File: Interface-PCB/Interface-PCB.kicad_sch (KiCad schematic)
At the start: 14 parts, among them J1 BARREL_JACK_PAD, J2 BARREL_JACK_PAD, J3 GPIO_DEBUG_HEADER, J4 RASPBERRYPI_GPIO_CONN_HEADER, J5 I2C_HEADER, M1 PERISTALTIC_PUMP, M2 PERISTALTIC_PUMP, M3 PERISTALTIC_PUMP, U1 TB6612FNG_BREAKOUT, U2 TB6612FNG_BREAKOUT

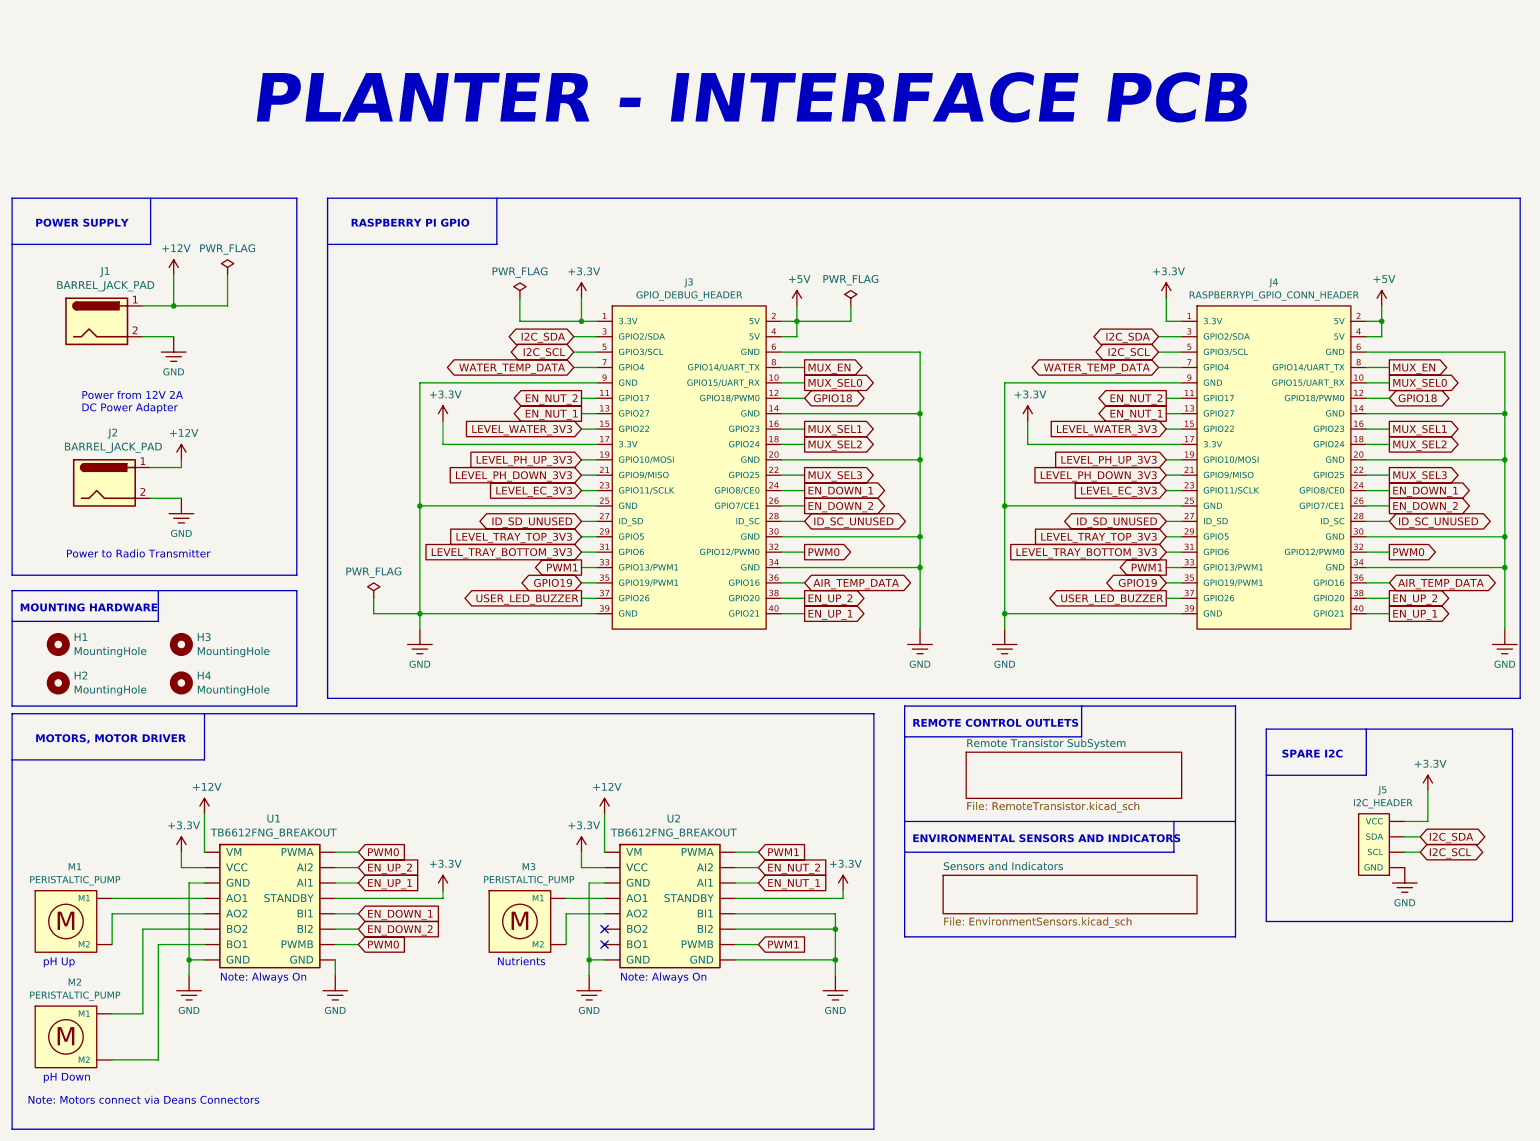
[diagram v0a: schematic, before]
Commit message: Update schematic based on breadboard tests
- Add current limiting resistors to Level Shifter output
- Add pull down resistors on all Mux outputs
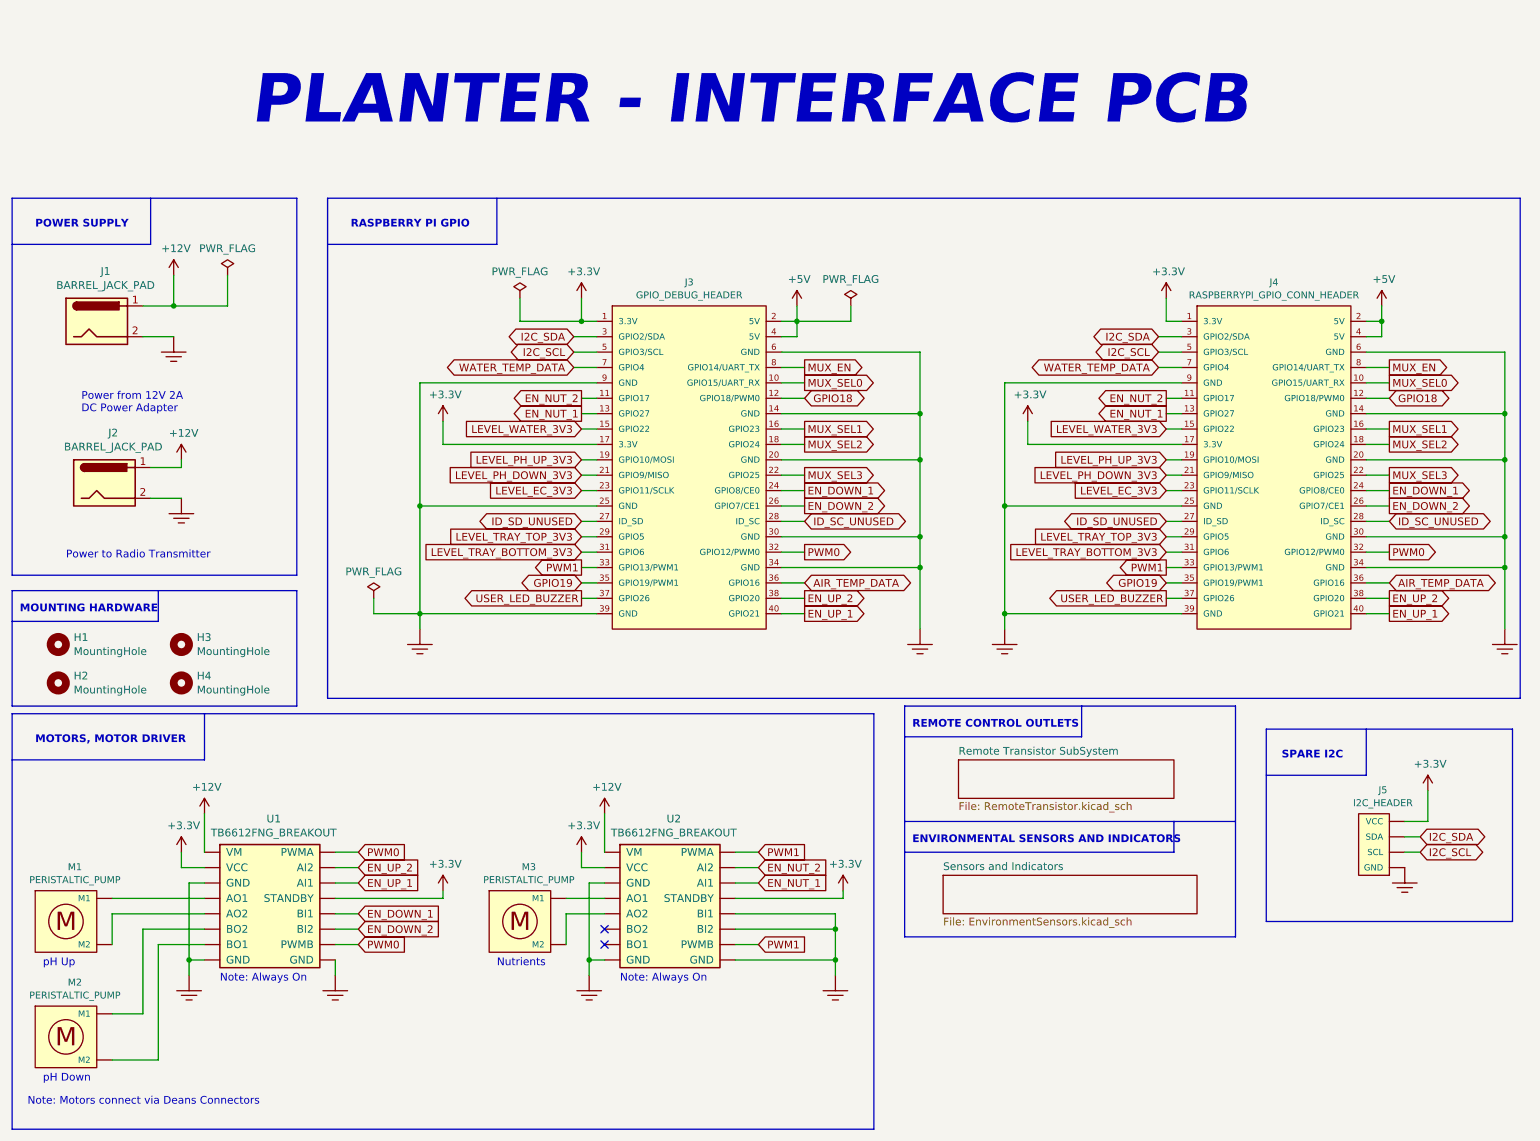
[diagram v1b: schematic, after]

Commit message: Add Planter Logo to schematic
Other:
- note added: "INTERFACE PCB"
- note removed: "PLANTER - INTERFACE PCB"
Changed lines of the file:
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@@
     (effects (font (size 1.27 1.27)) (justify left bottom))
   )
-  (text "PLANTER - INTERFACE PCB" (at 54.61 36.83 0)
+  (text "INTERFACE PCB" (at 93.98 38.1 0)
     (effects (font (size 8.001 8.001) (thickness 1.6002) bold italic) (justify left bottom))
   )
@@
     (pin "~")
   )
+  (symbol (lib_id "Interface-PCB:PLANTER_LOGO_8mm") (at 247.65 29.21 0) (unit 1)
+    (in_bom yes) (on_board yes) (fields_autoplaced)
+    (property "Reference" "#G1" (id 0) (at 247.65 17.3277 0)
+      (effects (font (size 1.27 1.27)) hide)
+    )
+    (property "Value" "PLANTER_LOGO_8mm" (id 1) (at 247.65 41.0923 0)
+      (effects (font (size 1.27 1.27)) hide)
+    )
+    (property "Footprint" "" (id 2) (at 247.65 29.21 0)
+      (effects (font (size 1.27 1.27)) hide)
+    )
+    (property "Datasheet" "" (id 3) (at 247.65 29.21 0)
+      (effects (font (size 1.27 1.27)) hide)
+    )
+  )
   (sheet (at 171.45 140.97) (size 35.56 6.35) (fields_autoplaced)
     (stroke (width 0) (type solid) (color 0 0 0 0))
@@
       (reference "#FLG04") (unit 1) (value "PWR_FLAG") (footprint "")
     )
+    (path "/6ae23f34-90ad-41bf-a46e-855f1c65bb29"
+      (reference "#G1") (unit 1) (value "PLANTER_LOGO_8mm") (footprint "")
+    )
     (path "/00000000-0000-0000-0000-000063fcc8a0"

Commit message: Add footprints for pads
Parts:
- J1, J2, M1, M2, M3: footprint TestPoint:TestPoint_2Pads_Pitch5.08mm_Drill1.3mm -> AA_Custom_Components:PowerPad_Pair_5.0x5.0mm
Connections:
- net at U1.4 (AO1): now also M1.1 (M1); no longer M1.7 (M1)
- net at U1.5 (AO2): now also M1.2 (M2); no longer M1.6 (M2)
- net at U1.6 (BO2): now also M2.1 (M1); no longer M2.7 (M1)
- net at U1.7 (BO1): now also M2.2 (M2); no longer M2.6 (M2)
- net at U2.4 (AO1): now also M3.1 (M1); no longer M3.7 (M1)
- net at U2.5 (AO2): now also M3.2 (M2); no longer M3.6 (M2)

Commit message: Add breakout board and IC footprints
- MUX
- Motor Driver
- PDIP ICs
- LEDs
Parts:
- U1, U2: footprint digikey-footprints:DIP-16_W7.62mm -> AA_Custom_Components:TB6612FNG_Breakout; Digikey_Part_Number (none) -> 1568-1755-ND; Manufacturer_Name (none) -> SparkFun
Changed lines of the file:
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@@
     (property "Reference" "U1" (id 0) (at 58.42 150.6982 0))
     (property "Value" "TB6612FNG_BREAKOUT" (id 1) (at 58.42 153.0096 0))
-    (property "Footprint" "digikey-footprints:DIP-16_W7.62mm" (id 2) (at 44.45 160.02 0)
+    (property "Footprint" "AA_Custom_Components:TB6612FNG_Breakout" (id 2) (at 44.45 160.02 0)
       (effects (font (size 1.27 1.27)) (justify left) hide)
     )
-    (property "Datasheet" "" (id 3) (at 62.23 160.02 0)
+    (property "Datasheet" "https://media.digikey.com/pdf/Data%20Sheets/Sparkfun%20PDFs/ROB-14450_Web.pdf" (id 3) (at 62.23 160.02 0)
+      (effects (font (size 1.27 1.27)) hide)
+    )
+    (property "Manufacturer_Name" "SparkFun" (id 4) (at 74.93 166.37 0)
+      (effects (font (size 1.27 1.27)) hide)
+    )
+    (property "Digikey_Part_Number" "1568-1755-ND" (id 5) (at 78.74 168.91 0)
       (effects (font (size 1.27 1.27)) hide)
     )
@@
     (property "Reference" "U2" (id 0) (at 124.46 150.6982 0))
     (property "Value" "TB6612FNG_BREAKOUT" (id 1) (at 124.46 153.0096 0))
-    (property "Footprint" "digikey-footprints:DIP-16_W7.62mm" (id 2) (at 110.49 160.02 0)
+    (property "Footprint" "AA_Custom_Components:TB6612FNG_Breakout" (id 2) (at 110.49 160.02 0)
       (effects (font (size 1.27 1.27)) (justify left) hide)
     )
-    (property "Datasheet" "" (id 3) (at 128.27 160.02 0)
+    (property "Datasheet" "https://media.digikey.com/pdf/Data%20Sheets/Sparkfun%20PDFs/ROB-14450_Web.pdf" (id 3) (at 128.27 160.02 0)
+      (effects (font (size 1.27 1.27)) hide)
+    )
+    (property "Manufacturer_Name" "SparkFun" (id 4) (at 140.97 166.37 0)
+      (effects (font (size 1.27 1.27)) hide)
+    )
+    (property "Digikey_Part_Number" "1568-1755-ND" (id 5) (at 144.78 168.91 0)
       (effects (font (size 1.27 1.27)) hide)
     )
@@
       (effects (font (size 1.27 1.27)) hide)
     )
-    (property "Datasheet" "~" (id 3) (at 30.48 69.596 0)
+    (property "Datasheet" "" (id 3) (at 30.48 69.596 0)
       (effects (font (size 1.27 1.27)) hide)
     )
@@
       (effects (font (size 1.27 1.27)) hide)
     )
-    (property "Datasheet" "~" (id 3) (at 31.75 96.266 0)
+    (property "Datasheet" "" (id 3) (at 31.75 96.266 0)
       (effects (font (size 1.27 1.27)) hide)
     )
@@
     )
     (path "/00000000-0000-0000-0000-00006375997b/00000000-0000-0000-0000-000063bcadd9"
-      (reference "D2") (unit 1) (value "12V_ON_SMD") (footprint "LED_SMD:LED_1206_3216Metric_Pad1.42x1.75mm_HandSolder")
+      (reference "D2") (unit 1) (value "12V_ON_SMD") (footprint "AA_Custom_Components:LED_SS_1206_3216Metric_Pad1.42x1.75mm_HandSolder")
     )
     (path "/00000000-0000-0000-0000-00006375997b/00000000-0000-0000-0000-000063c002c0"
@@
     )
     (path "/00000000-0000-0000-0000-00006375997b/00000000-0000-0000-0000-000063c002c6"
-      (reference "D4") (unit 1) (value "USER_LED_SMD") (footprint "LED_SMD:LED_1206_3216Metric_Pad1.42x1.75mm_HandSolder")
+      (reference "D4") (unit 1) (value "USER_LED_SMD") (footprint "AA_Custom_Components:LED_SS_1206_3216Metric_Pad1.42x1.75mm_HandSolder")
     )
     (path "/00000000-0000-0000-0000-00006375997b/00000000-0000-0000-0000-000063bc8549"
@@
     )
     (path "/00000000-0000-0000-0000-00006375997b/00000000-0000-0000-0000-000063bcaddf"
-      (reference "D6") (unit 1) (value "5V_ON_SMD") (footprint "LED_SMD:LED_1206_3216Metric_Pad1.42x1.75mm_HandSolder")
+      (reference "D6") (unit 1) (value "5V_ON_SMD") (footprint "AA_Custom_Components:LED_SS_1206_3216Metric_Pad1.42x1.75mm_HandSolder")
     )
     (path "/00000000-0000-0000-0000-000063bd3cac"
@@
     )
     (path "/00000000-0000-0000-0000-00006375997b/00000000-0000-0000-0000-000063be02c6"
-      (reference "IC1") (unit 1) (value "SN74LVC245AN") (footprint "Package_DIP:DIP-20_W7.62mm_LongPads")
-    )
-    (path "/00000000-0000-0000-0000-00006373d3ae/00000000-0000-0000-0000-00006380380b"
-      (reference "IC2") (unit 1) (value "TBD62783A") (footprint "Package_DIP:DIP-18_W7.62mm_LongPads")
-    )
-    (path "/00000000-0000-0000-0000-00006373d3ae/00000000-0000-0000-0000-0000638228b4"
-      (reference "IC3") (unit 1) (value "TBD62783A") (footprint "Package_DIP:DIP-18_W7.62mm_LongPads")
+      (reference "IC1") (unit 1) (value "SN74LVC245AN") (footprint "AA_Custom_Components:DIP-20_W7.62mm_Socket_IC")
+    )
+    (path "/00000000-0000-0000-0000-00006373d3ae/0381685e-7299-4035-89b8-dc29eac2e5c3"
+      (reference "IC2") (unit 1) (value "TBD62783APG") (footprint "AA_Custom_Components:DIP-18_W7.62mm_Socket_IC")
+    )
+    (path "/00000000-0000-0000-0000-00006373d3ae/5adcc529-5723-4cd5-ab40-31266024c46e"
+      (reference "IC3") (unit 1) (value "TBD62783APG") (footprint "AA_Custom_Components:DIP-18_W7.62mm_Socket_IC")
     )
     (path "/00000000-0000-0000-0000-000063af14b6"
@@
     )
     (path "/00000000-0000-0000-0000-0000638d4504"
-      (reference "U1") (unit 1) (value "TB6612FNG_BREAKOUT") (footprint "digikey-footprints:DIP-16_W7.62mm")
+      (reference "U1") (unit 1) (value "TB6612FNG_BREAKOUT") (footprint "AA_Custom_Components:TB6612FNG_Breakout")
     )
     (path "/00000000-0000-0000-0000-000063a48f27"
-      (reference "U2") (unit 1) (value "TB6612FNG_BREAKOUT") (footprint "digikey-footprints:DIP-16_W7.62mm")
-    )
-    (path "/00000000-0000-0000-0000-00006373d3ae/00000000-0000-0000-0000-000063bc18a1"
-      (reference "U3") (unit 1) (value "CD74HC4067_MUX") (footprint "digikey-footprints:Socket_DIP-24_15.24mm_Conn")
-    )
-  )
+      (reference "U2") (unit 1) (value "TB6612FNG_BREAKOUT") (footprint "AA_Custom_Components:TB6612FNG_Breakout")
+    )
+    (path "/00000000-0000-0000-0000-00006373d3ae/ec774a0e-a2b2-42d0-8de4-8aedd11eddac"
+      (reference "U3") (unit 1) (value "CD74HC4067_MUX_BREAKOUT") (footprint "AA_Custom_Components:CD74HC4067_MUX_BREAKOUT")
+    )
+  )

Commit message: Add JST Connector Footprints
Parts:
- J5: footprint Connector_JST:JST_XH_B4B-XH-A_1x04_P2.50mm_Vertical -> AA_Custom_Components:JST_XH_1x04_P2.54mm_Vertical
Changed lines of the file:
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@@
       (effects (font (size 1.143 1.143)))
     )
-    (property "Footprint" "Connector_JST:JST_XH_B4B-XH-A_1x04_P2.50mm_Vertical" (id 2) (at 242.57 146.05 0)
+    (property "Footprint" "AA_Custom_Components:JST_XH_1x04_P2.54mm_Vertical" (id 2) (at 242.57 146.05 0)
       (effects (font (size 0.508 0.508)) hide)
     )
@@
     )
     (path "/00000000-0000-0000-0000-00006375997b/00000000-0000-0000-0000-000063bb536f"
-      (reference "C1") (unit 1) (value "100nF") (footprint "Capacitor_THT:C_Disc_D3.4mm_W2.1mm_P2.50mm")
+      (reference "C1") (unit 1) (value "100nF") (footprint "AA_Custom_Components:C_Ceramic_Disc_D4.3mm_W1.9mm_P5.08mm")
     )
     (path "/00000000-0000-0000-0000-00006373d3ae/00000000-0000-0000-0000-000063bbebc5"
-      (reference "C2") (unit 1) (value "100nF") (footprint "Capacitor_THT:C_Disc_D3.4mm_W2.1mm_P2.50mm")
+      (reference "C2") (unit 1) (value "100nF") (footprint "AA_Custom_Components:C_Ceramic_Disc_D4.3mm_W1.9mm_P5.08mm")
     )
     (path "/00000000-0000-0000-0000-00006373d3ae/00000000-0000-0000-0000-000063bc1dbe"
-      (reference "C3") (unit 1) (value "100nF") (footprint "Capacitor_THT:C_Disc_D3.4mm_W2.1mm_P2.50mm")
+      (reference "C3") (unit 1) (value "100nF") (footprint "AA_Custom_Components:C_Ceramic_Disc_D4.3mm_W1.9mm_P5.08mm")
     )
     (path "/00000000-0000-0000-0000-00006375997b/00000000-0000-0000-0000-000063bc6500"
@@
     )
     (path "/00000000-0000-0000-0000-00006382f956"
-      (reference "J5") (unit 1) (value "I2C_HEADER") (footprint "Connector_JST:JST_XH_B4B-XH-A_1x04_P2.50mm_Vertical")
+      (reference "J5") (unit 1) (value "I2C_HEADER") (footprint "AA_Custom_Components:JST_XH_1x04_P2.54mm_Vertical")
     )
     (path "/00000000-0000-0000-0000-00006375997b/00000000-0000-0000-0000-0000637638f0"
-      (reference "J6") (unit 1) (value "LEVEL_SENSOR") (footprint "Connector_JST:JST_XH_B3B-XH-A_1x03_P2.50mm_Vertical")
+      (reference "J6") (unit 1) (value "LEVEL_SENSOR") (footprint "AA_Custom_Components:JST_XH_1x03_P2.54mm_Vertical")
     )
     (path "/00000000-0000-0000-0000-00006375997b/00000000-0000-0000-0000-0000637638e5"
-      (reference "J7") (unit 1) (value "LEVEL_SENSOR") (footprint "Connector_JST:JST_XH_B3B-XH-A_1x03_P2.50mm_Vertical")
+      (reference "J7") (unit 1) (value "LEVEL_SENSOR") (footprint "AA_Custom_Components:JST_XH_1x03_P2.54mm_Vertical")
     )
     (path "/00000000-0000-0000-0000-00006375997b/00000000-0000-0000-0000-000063763962"
-      (reference "J8") (unit 1) (value "LEVEL_SENSOR") (footprint "Connector_JST:JST_XH_B3B-XH-A_1x03_P2.50mm_Vertical")
+      (reference "J8") (unit 1) (value "LEVEL_SENSOR") (footprint "AA_Custom_Components:JST_XH_1x03_P2.54mm_Vertical")
     )
     (path "/00000000-0000-0000-0000-00006375997b/00000000-0000-0000-0000-0000637638bf"
-      (reference "J9") (unit 1) (value "LEVEL_SENSOR") (footprint "Connector_JST:JST_XH_B3B-XH-A_1x03_P2.50mm_Vertical")
+      (reference "J9") (unit 1) (value "LEVEL_SENSOR") (footprint "AA_Custom_Components:JST_XH_1x03_P2.54mm_Vertical")
     )
     (path "/00000000-0000-0000-0000-00006375997b/00000000-0000-0000-0000-0000637638d2"
-      (reference "J10") (unit 1) (value "LEVEL_SENSOR") (footprint "Connector_JST:JST_XH_B3B-XH-A_1x03_P2.50mm_Vertical")
+      (reference "J10") (unit 1) (value "LEVEL_SENSOR") (footprint "AA_Custom_Components:JST_XH_1x03_P2.54mm_Vertical")
     )
     (path "/00000000-0000-0000-0000-00006375997b/00000000-0000-0000-0000-00006376394d"
-      (reference "J11") (unit 1) (value "LEVEL_SENSOR") (footprint "Connector_JST:JST_XH_B3B-XH-A_1x03_P2.50mm_Vertical")
+      (reference "J11") (unit 1) (value "LEVEL_SENSOR") (footprint "AA_Custom_Components:JST_XH_1x03_P2.54mm_Vertical")
     )
     (path "/00000000-0000-0000-0000-00006375997b/00000000-0000-0000-0000-000063763918"
-      (reference "J12") (unit 1) (value "TEMPERATURE_SENSOR") (footprint "Connector_JST:JST_XH_B3B-XH-A_1x03_P2.50mm_Vertical")
+      (reference "J12") (unit 1) (value "TEMPERATURE_SENSOR") (footprint "AA_Custom_Components:JST_XH_1x03_P2.54mm_Vertical")
     )
     (path "/00000000-0000-0000-0000-00006375997b/00000000-0000-0000-0000-00006376390b"
-      (reference "J13") (unit 1) (value "TEMPERATURE_SENSOR") (footprint "Connector_JST:JST_XH_B3B-XH-A_1x03_P2.50mm_Vertical")
+      (reference "J13") (unit 1) (value "TEMPERATURE_SENSOR") (footprint "AA_Custom_Components:JST_XH_1x03_P2.54mm_Vertical")
     )
     (path "/00000000-0000-0000-0000-00006373d3ae/00000000-0000-0000-0000-00006375cc97"
-      (reference "J14") (unit 1) (value "CONN_05JST") (footprint "Connector_JST:JST_XH_B5B-XH-A_1x05_P2.50mm_Vertical")
+      (reference "J14") (unit 1) (value "CONN_05JST") (footprint "AA_Custom_Components:JST_XH_1x05_P2.54mm_Vertical")
     )
     (path "/00000000-0000-0000-0000-00006373d3ae/00000000-0000-0000-0000-0000638228aa"
-      (reference "J15") (unit 1) (value "CONN_05JST") (footprint "Connector_JST:JST_XH_B5B-XH-A_1x05_P2.50mm_Vertical")
+      (reference "J15") (unit 1) (value "CONN_05JST") (footprint "AA_Custom_Components:JST_XH_1x05_P2.54mm_Vertical")
     )
     (path "/00000000-0000-0000-0000-0000638d58ae"

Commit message: Update Header pin and Buzzer Footprints
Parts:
- J3, J4: footprint Connector_PinHeader_2.54mm:PinHeader_2x21_P2.54mm_Vertical -> AA_Custom_Components:RASPBERRYPI-40-PIN-GPIO-2x20_P2.54mm_Vertical
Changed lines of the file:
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@@
       (effects (font (size 1.143 1.143)))
     )
-    (property "Footprint" "Connector_PinHeader_2.54mm:PinHeader_2x21_P2.54mm_Vertical" (id 2) (at 223.52 63.5 0)
+    (property "Footprint" "AA_Custom_Components:RASPBERRYPI-40-PIN-GPIO-2x20_P2.54mm_Vertical" (id 2) (at 223.52 63.5 0)
       (effects (font (size 0.508 0.508)) hide)
     )
@@
       (effects (font (size 1.143 1.143)))
     )
-    (property "Footprint" "Connector_PinHeader_2.54mm:PinHeader_2x21_P2.54mm_Vertical" (id 2) (at 127 63.5 0)
+    (property "Footprint" "AA_Custom_Components:RASPBERRYPI-40-PIN-GPIO-2x20_P2.54mm_Vertical" (id 2) (at 127 63.5 0)
       (effects (font (size 0.508 0.508)) hide)
     )
@@
     )
     (path "/00000000-0000-0000-0000-00006375997b/00000000-0000-0000-0000-000063bf8b85"
-      (reference "BZ1") (unit 1) (value "Buzzer") (footprint "Buzzer_Beeper:Buzzer_TDK_PS1240P02BT_D12.2mm_H6.5mm")
+      (reference "BZ1") (unit 1) (value "Buzzer") (footprint "AA_Custom_Components:Buzzer_Generic_D12.2mm_H6.5mm")
     )
     (path "/00000000-0000-0000-0000-00006375997b/00000000-0000-0000-0000-000063bb536f"
@@
     )
     (path "/00000000-0000-0000-0000-000063ceadab"
-      (reference "J3") (unit 1) (value "GPIO_DEBUG_HEADER") (footprint "Connector_PinHeader_2.54mm:PinHeader_2x21_P2.54mm_Vertical")
+      (reference "J3") (unit 1) (value "GPIO_DEBUG_HEADER") (footprint "AA_Custom_Components:RASPBERRYPI-40-PIN-GPIO-2x20_P2.54mm_Vertical")
     )
     (path "/00000000-0000-0000-0000-0000637562be"
-      (reference "J4") (unit 1) (value "RASPBERRYPI_GPIO_CONN_HEADER") (footprint "Connector_PinHeader_2.54mm:PinHeader_2x21_P2.54mm_Vertical")
+      (reference "J4") (unit 1) (value "RASPBERRYPI_GPIO_CONN_HEADER") (footprint "AA_Custom_Components:RASPBERRYPI-40-PIN-GPIO-2x20_P2.54mm_Vertical")
     )
     (path "/00000000-0000-0000-0000-00006382f956"
